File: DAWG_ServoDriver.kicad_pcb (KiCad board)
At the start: 2 copper layers, 154 parts, among them CN1 Conn_02x19_Odd_Even, CN2 Conn_02x19_Odd_Even, IC1 DRV8251ADDAR, IC2 DRV8251ADDAR, IC3 DRV8251ADDAR, IC4 DRV8251ADDAR, J1 Conn_01x05, J10 Screw_Terminal_01x02, J11 Conn_01x10, J12 Conn_01x08, J13 Conn_01x05, J14 Conn_01x06, J15 Conn_01x08, J16 Screw_Terminal_01x02, J17 Conn_01x03, J18 Conn_01x03, J19 Conn_01x03, J2 Screw_Terminal_01x02, J20 Conn_01x03, J21 Conn_01x03, J22 Conn_01x03, J23 Conn_01x03, J24 Conn_01x03, J25 Conn_01x03, J26 Conn_01x03, J27 Conn_01x03, J28 Conn_01x03, J29 Conn_01x03, J3 Conn_01x05, J30 Conn_01x03, J31 Conn_01x03, J32 Conn_01x03, J33 Conn_01x03, J34 Conn_01x03, J35 Conn_01x03, J4 Conn_01x04_Pin, J5 Screw_Terminal_01x02, J6 Conn_01x03, J7 Screw_Terminal_01x02, J8 Screw_Terminal_01x02, J9 Conn_01x05, Q1 BSS138, Q10 BSS138, Q11 BSS138, Q12 BSS138, Q13 BSS138, Q14 BSS138, Q15 BSS138, Q16 BSS138, Q17 BSS138, Q18 BSS138, Q19 BSS138, Q2 BSS138, Q20 BSS138, Q3 BSS138, Q4 BSS138, Q5 BSS138, Q6 BSS138, Q7 BSS138, Q8 BSS138, Q9 BSS138, SW1 SW_Push, U1 TPS62177DQC, U2 STM32G431C8Tx, U3 LD1117S12TR_SOT223, U4 ICM-20602, U5 ICM-20602, Y1 Crystal_GND24

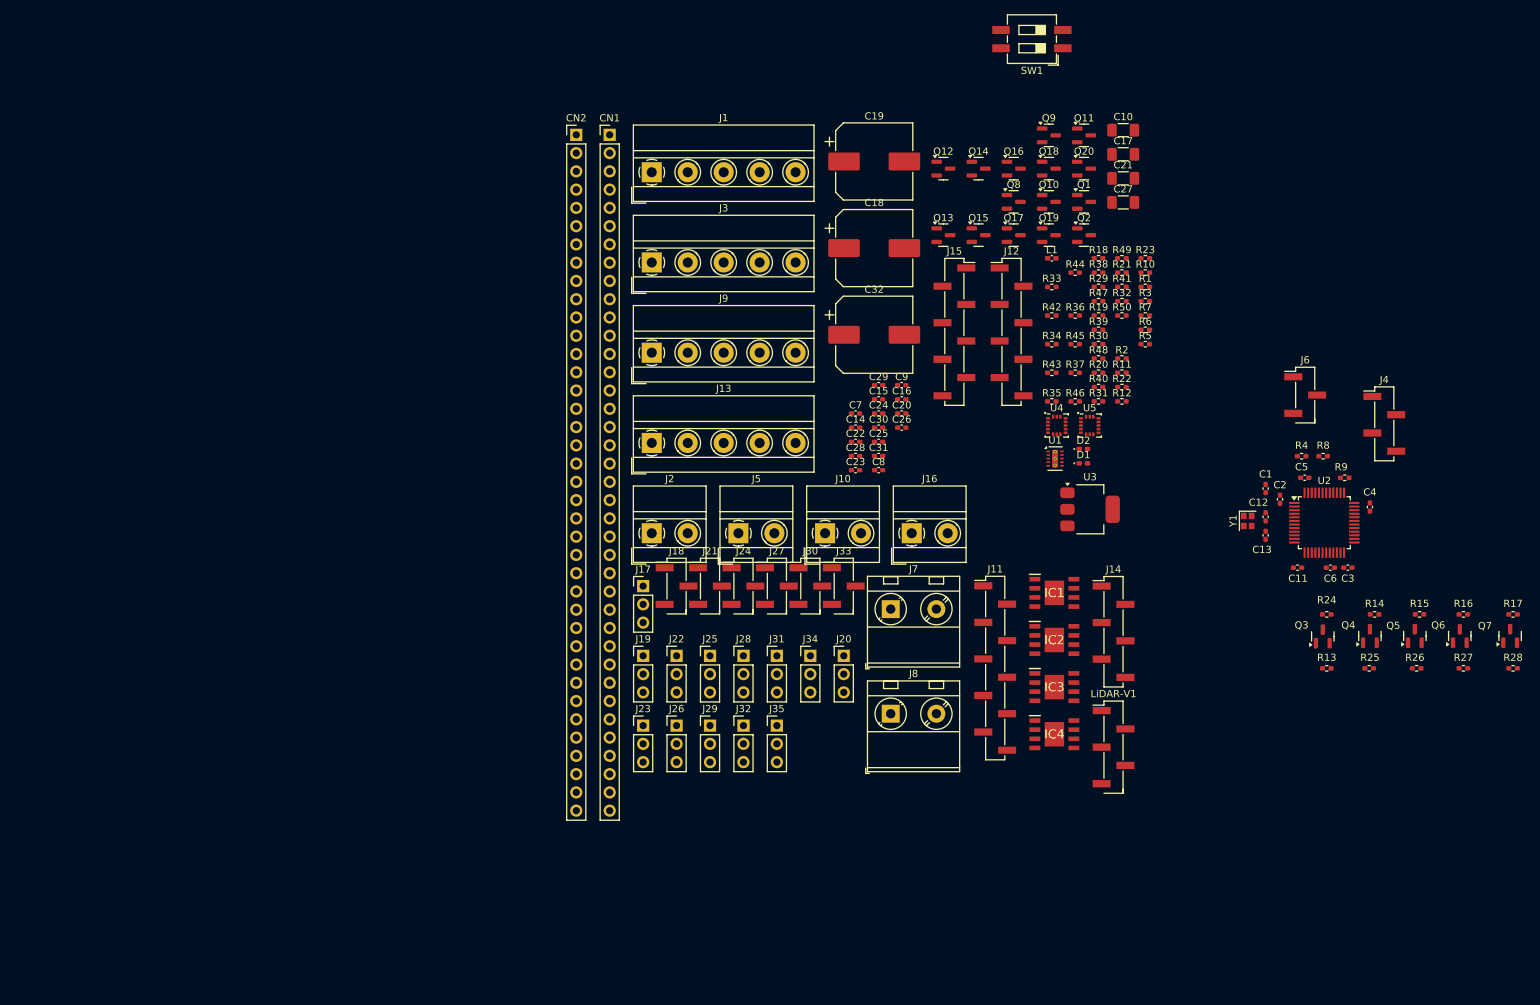
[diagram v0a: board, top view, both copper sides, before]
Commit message: Placed mos most components, routed servo.
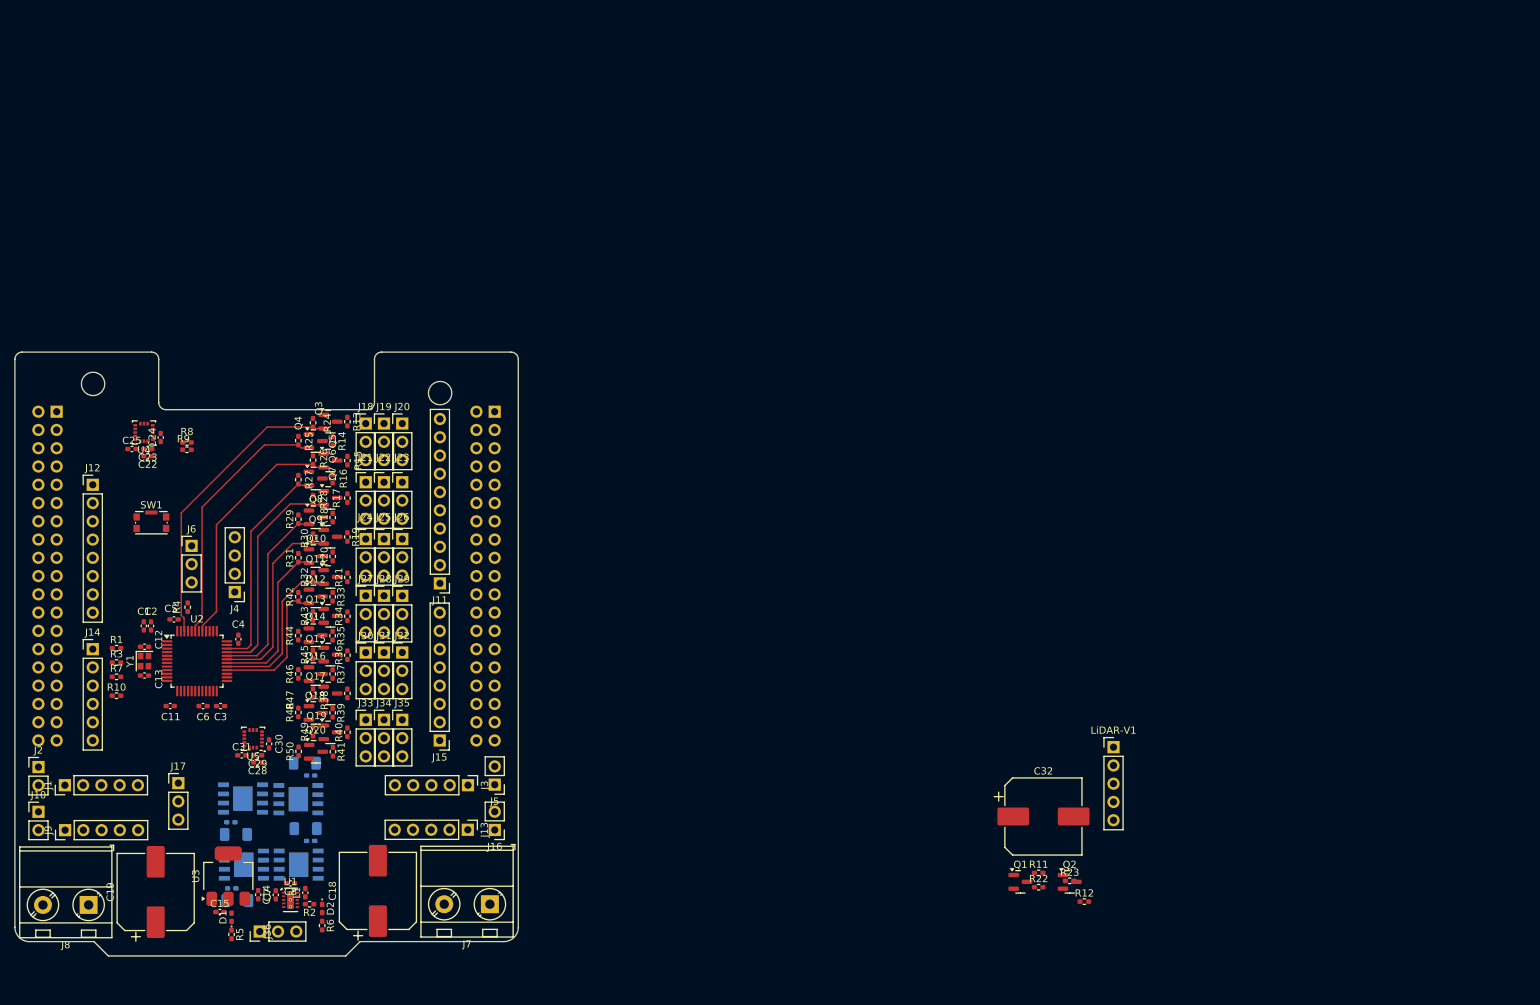
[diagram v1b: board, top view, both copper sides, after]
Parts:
- removed CN1, CN2: Conn_02x19_Odd_Even, Connector_PinHeader_2.54mm:PinHeader_1x38_P2.54mm_Vertical
- added CN10: Conn_02x19_Odd_Even, Connector_PinHeader_2.54mm:PinHeader_2x19_P2.54mm_Vertical, B.Cu at (89.8, 82.3)
- added CN7: Conn_02x19_Odd_Even, Connector_PinHeader_2.54mm:PinHeader_2x19_P2.54mm_Vertical, B.Cu at (28.9, 82.3)
- added J36: Conn_01x03, Connector_PinHeader_2.54mm:PinHeader_1x03_P2.54mm_Vertical, F.Cu at (57.1, 154.6)
- C10, C16, C17, C20, C21, C26, C27, C9, IC1, IC2, IC3, IC4: moved to B.Cu
- J1, J13, J3, J9: footprint TerminalBlock_MetzConnect:TerminalBlock_MetzConnect_Type011_RT05505HBWC_1x05_P5.00mm_Horizontal -> Connector_PinHeader_2.54mm:PinHeader_1x05_P2.54mm_Vertical
- J10, J16, J2, J5: footprint TerminalBlock_MetzConnect:TerminalBlock_MetzConnect_Type011_RT05502HBWC_1x02_P5.00mm_Horizontal -> Connector_PinHeader_2.54mm:PinHeader_1x02_P2.54mm_Vertical
- J11: footprint Connector_PinHeader_2.54mm:PinHeader_1x10_P2.54mm_Vertical_SMD_Pin1Left -> Connector_PinHeader_2.54mm:PinHeader_1x10_P2.54mm_Vertical
- J12: footprint Connector_PinHeader_2.54mm:PinHeader_1x08_P2.54mm_Vertical_SMD_Pin1Left -> Connector_PinHeader_2.54mm:PinHeader_1x08_P2.54mm_Vertical
- J14: footprint Connector_PinHeader_2.54mm:PinHeader_1x06_P2.54mm_Vertical_SMD_Pin1Left -> Connector_PinHeader_2.54mm:PinHeader_1x06_P2.54mm_Vertical
- J15: footprint Connector_PinHeader_2.54mm:PinHeader_1x08_P2.54mm_Vertical_SMD_Pin1Right -> Connector_PinHeader_2.54mm:PinHeader_1x08_P2.54mm_Vertical
- J18, J21, J24, J27, J30, J33, J6: footprint Connector_PinHeader_2.54mm:PinHeader_1x03_P2.54mm_Vertical_SMD_Pin1Left -> Connector_PinHeader_2.54mm:PinHeader_1x03_P2.54mm_Vertical
- J4: footprint Connector_PinHeader_2.54mm:PinHeader_1x04_P2.54mm_Vertical_SMD_Pin1Left -> Connector_PinHeader_2.54mm:PinHeader_1x04_P2.54mm_Vertical
- LiDAR-V1: footprint Connector_PinHeader_2.54mm:PinHeader_1x05_P2.54mm_Vertical_SMD_Pin1Left -> Connector_PinHeader_2.54mm:PinHeader_1x05_P2.54mm_Vertical
- SW1: footprint Button_Switch_SMD:SW_DIP_SPSTx02_Slide_6.7x6.64mm_W8.61mm_P2.54mm_LowProfile -> Button_Switch_SMD:SW_Push_1P1T-SH_NO_CK_KMR2xxG
- moved R28 168.5 mm to (64.5, 94.5), turned to 90 degrees
- moved Q7 165.2 mm to (67.0, 94.3), turned to 0 degrees
- moved R27 164.1 mm to (62.5, 91.8), turned to 90 degrees
- moved R17 162.9 mm to (69.3, 94.3), turned to -90 degrees
- moved J4 161.6 mm to (53.6, 107.4), turned to 180 degrees
- moved R9 161.0 mm to (47.0, 87.6)
- moved Q6 160.6 mm to (64.9, 91.6), turned to 0 degrees
- moved C21 159.0 mm to (54.0, 150.3), turned to 180 degrees
- moved C5 158.5 mm to (45.2, 111.2)
- moved C4 158.4 mm to (54.1, 114.0)
- moved R16 158.4 mm to (67.3, 91.6), turned to 90 degrees
- moved R8 158.0 mm to (47.0, 86.6)
- moved C2 158.0 mm to (42.0, 112.1)
- moved C11 157.9 mm to (44.7, 123.2)
- moved C3 157.9 mm to (51.7, 123.2)
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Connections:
- IC1 pad 1: /ADC1/14 -> /IsenseM1
- IC2 pad 1: /ADC1/15 -> /IsenseM2
- IC3 pad 1: /ADC1/9 -> /IsenseM3
- IC4 pad 1: /ADC1/7 -> /IsenseM4
- J11 pad 1: /PWM1/2_M3 -> Net-(CN10-Pin_21)
- J11 pad 3: /PWM4/1_M2 -> /Mtr1_EncoderB
- J11 pad 4: /ADC1/7 -> /PWM3/1_M1
- J11 pad 5: /PWM3/1_M1 -> /PWM2/1_M1
- J11 pad 6: /PWM2/1_M1 -> /Mtr1_EncoderA
- J11 pad 7: Net-(CN1-Pin_9) -> GND
- J14 pad 1: /PWM2/1 -> /IsenseM1
- J14 pad 2: /PWM2/2 -> /IsenseM2
- J14 pad 3: Net-(CN2-Pin_32) -> /IsenseM3
- J14 pad 4: /PWM1/2N -> /IsenseM4
- J15 pad 1: Net-(CN1-Pin_37) -> /IMU1_INT
- J15 pad 2: Net-(CN1-Pin_35) -> /IMU2_INT
- J15 pad 3: /Mtr3_EncoderA -> Net-(CN10-Pin_33)
- J15 pad 4: /Mtr3_EncoderB -> /Mtr2_EncoderB
- J15 pad 5: /PWM3/2_M4 -> /Mtr2_EncoderA
- J15 pad 6: /Mtr3_EncoderZ -> /PWM4/1_M2
- J15 pad 7: /PWM2/3_M4 -> Net-(CN10-Pin_25)
- J15 pad 8: /PWM1/1_M3 -> Net-(CN10-Pin_23)
- Q10 pad 2: /PWM2/4 -> /PWM1/1
- Q11 pad 2: /PWM3/1 -> /PWM15/2
- Q12 pad 2: /PWM3/2 -> /PWM15/1
- Q15 pad 2: /PWM4/1 -> Net-(Q15-S)
- Q16 pad 2: /PWM4/2 -> Net-(Q16-S)
- Q17 pad 2: /PWM4/4 -> Net-(Q17-S)
- Q18 pad 2: /PWM15/1 -> Net-(Q18-S)
- Q19 pad 2: /PWM15/2 -> Net-(Q19-S)
- Q20 pad 2: /PWM16/1 -> Net-(Q20-S)
- Q3 pad 2: /PWM1/1 -> /PWM4/4
- Q4 pad 2: /PWM1/2 -> /PWM4/1
- Q5 pad 2: /PWM1/3 -> /PWM16/1
- Q6 pad 2: /PWM1/4 -> /PWM4/2
- Q7 pad 2: /PWM2/1 -> /PWM1/4
- Q8 pad 2: /PWM2/2 -> /PWM1/3
- Q9 pad 2: /PWM2/3 -> /PWM1/2
- R1 pad 2: /ADC1/14 -> /IsenseM1
- R10 pad 2: /ADC1/7 -> /IsenseM4
- R24 pad 1: /PWM1/1 -> /PWM4/4
- R25 pad 1: /PWM1/2 -> /PWM4/1
- R26 pad 1: /PWM1/3 -> /PWM16/1
- R27 pad 1: /PWM1/4 -> /PWM4/2
- R28 pad 1: /PWM2/1 -> /PWM1/4
- R29 pad 1: /PWM2/2 -> /PWM1/3
- R3 pad 2: /ADC1/15 -> /IsenseM2
- R30 pad 1: /PWM2/3 -> /PWM1/2
- R31 pad 1: /PWM2/4 -> /PWM1/1
- R32 pad 1: /PWM3/1 -> /PWM15/2
- R42 pad 1: /PWM3/2 -> /PWM15/1
- R45 pad 1: /PWM4/1 -> Net-(Q15-S)
- R46 pad 1: /PWM4/2 -> Net-(Q16-S)
- R47 pad 1: /PWM4/4 -> Net-(Q17-S)
- R48 pad 1: /PWM15/1 -> Net-(Q18-S)
- R49 pad 1: /PWM15/2 -> Net-(Q19-S)
- R50 pad 1: /PWM16/1 -> Net-(Q20-S)
- R7 pad 2: /ADC1/9 -> /IsenseM3
- U2 pad 11: /PWM15/2 -> unconnected-(U2-PA3-Pad11)
- U2 pad 15: /PWM1/1 -> unconnected-(U2-PA7-Pad15)
- U2 pad 29: unconnected-(U2-PB15-Pad29) -> /PWM15/2
- U2 pad 30: /I2C3_SCL -> /PWM1/1
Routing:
- net /PWM4/4: track 0.00 -> 41.5 mm
- net /PWM4/1: track 0.00 -> 36.3 mm
- net /PWM16/1: track 0.00 -> 34.2 mm
- net /PWM1/4: track 0.00 -> 31.8 mm
- net /PWM4/2: track 0.00 -> 30.2 mm
- net /PWM1/2: track 0.00 -> 26.9 mm
- net /PWM1/3: track 0.00 -> 26.4 mm
- net /PWM1/1: track 0.00 -> 22.9 mm
- net /PWM15/2: track 0.00 -> 22.8 mm
- net /PWM15/1: track 0.00 -> 19.7 mm
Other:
- board outline added: 70 x 84 mm
- board text added: "STM32 Morpho"
- board text added: "®©®"

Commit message: Finished Routing all except IMU2_INT and GNDs
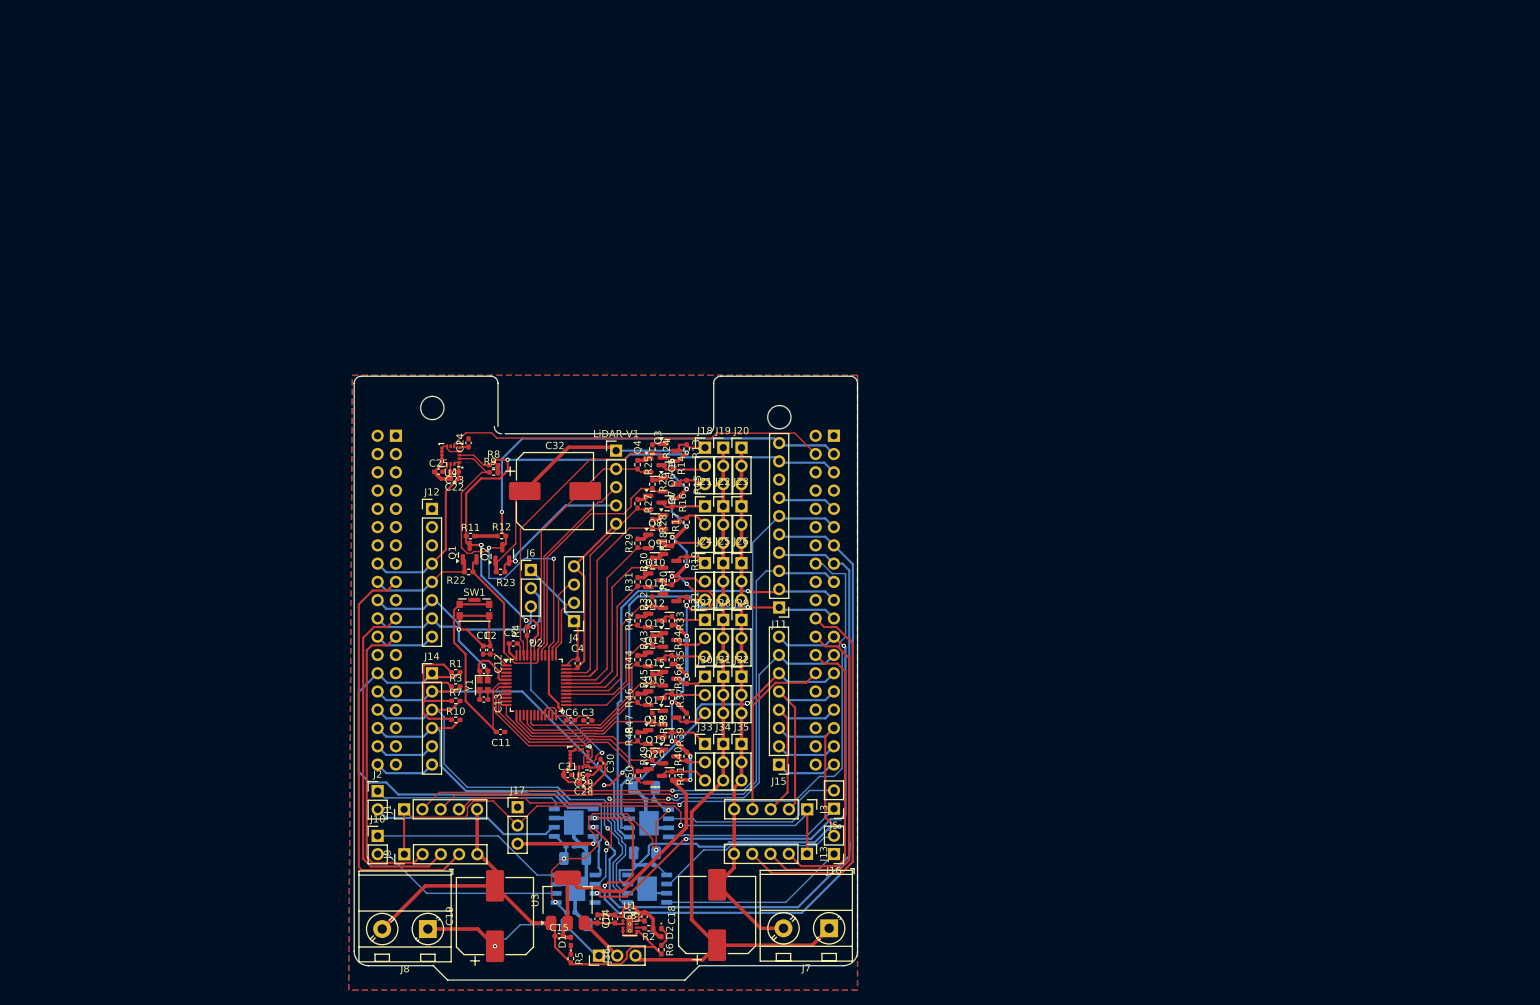
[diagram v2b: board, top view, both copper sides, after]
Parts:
- moved R12 95.7 mm to (90.8, 99.6), turned to 180 degrees
- moved R11 91.9 mm to (86.4, 99.6)
- moved Q2 91.1 mm to (90.8, 102.1), turned to 90 degrees
- moved R22 90.6 mm to (86.2, 104.6), turned to 180 degrees
- moved R23 90.1 mm to (90.6, 104.6), turned to 180 degrees
- moved Q1 89.2 mm to (86.3, 101.9), turned to 90 degrees
- moved C32 81.6 mm to (98.2, 93.3)
- moved LiDAR-V1 80.5 mm to (106.7, 87.7)
- moved C3 51.1 mm to (102.8, 125.2)
- moved C6 51.1 mm to (100.3, 125.2)
- moved IC2 48.9 mm to (111.2, 139.5)
- moved IC4 48.6 mm to (111.0, 148.6)
- moved Q3 47.3 mm to (114.1, 87.8)
- moved J4 47.3 mm to (100.8, 111.4)
- moved R13 47.3 mm to (116.5, 87.5)
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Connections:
- CN10 pad 19: /PWM3/2_M2 -> /PWM4/1_M2
- CN10 pad 2: unconnected-(CN10-Pin_2-Pad2) -> /IMU2_INT
- CN10 pad 21: Net-(CN10-Pin_21) -> /PWM1/2_M3
- CN10 pad 22: unconnected-(CN10-Pin_22-Pad22) -> /Mtr4_EncoderZ
- CN10 pad 23: Net-(CN10-Pin_23) -> /PWM1/1_M3
- CN10 pad 24: unconnected-(CN10-Pin_24-Pad24) -> /Mtr4_EncoderB
- CN10 pad 25: Net-(CN10-Pin_25) -> /PWM2/3_M4
- CN10 pad 26: unconnected-(CN10-Pin_26-Pad26) -> /Mtr4_EncoderA
- CN10 pad 27: /PWM4/1_M2 -> /PWM3/2_M2
- CN10 pad 28: unconnected-(CN10-Pin_28-Pad28) -> /Mtr2_EncoderZ
- CN10 pad 33: Net-(CN10-Pin_33) -> /PWM3/2_M4
- CN10 pad 35: /IMU2_INT -> Net-(CN10-Pin_35)
- CN10 pad 37: /IMU1_INT -> Net-(CN10-Pin_37)
- CN10 pad 4: unconnected-(CN10-Pin_4-Pad4) -> /IMU1_INT
- CN7 pad 17: /Mtr4_EncoderA -> /Mtr3_EncoderZ
- CN7 pad 21: /Mtr4_EncoderB -> /Mtr3_EncoderB
- CN7 pad 23: /Mtr4_EncoderZ -> /Mtr3_EncoderA
- CN7 pad 32: /IsenseM3 -> /IsenseM4
- CN7 pad 34: /IsenseM4 -> /IsenseM3
- J11 pad 1: Net-(CN10-Pin_21) -> /PWM1/2_M3
- J11 pad 2: /PWM3/2_M2 -> /PWM4/1_M2
- J14 pad 3: /IsenseM3 -> /IsenseM4
- J14 pad 4: /IsenseM4 -> /IsenseM3
- J15 pad 1: /IMU1_INT -> Net-(CN10-Pin_37)
- J15 pad 2: /IMU2_INT -> Net-(CN10-Pin_35)
- J15 pad 3: Net-(CN10-Pin_33) -> /PWM3/2_M4
- J15 pad 6: /PWM4/1_M2 -> /PWM3/2_M2
- J15 pad 7: Net-(CN10-Pin_25) -> /PWM2/3_M4
- J15 pad 8: Net-(CN10-Pin_23) -> /PWM1/1_M3
- Q13 pad 2: /PWM3/3 -> /PWM2/4
- Q15 pad 2: Net-(Q15-S) -> /PWM3/3
- Q16 pad 2: Net-(Q16-S) -> /PWM3/1
- Q17 pad 2: Net-(Q17-S) -> /PWM2/1
- Q18 pad 2: Net-(Q18-S) -> /PWM3/2
- Q19 pad 2: Net-(Q19-S) -> /PWM2/3
- Q20 pad 2: Net-(Q20-S) -> /PWM2/2
- R43 pad 1: /PWM3/3 -> /PWM2/4
- R45 pad 1: Net-(Q15-S) -> /PWM3/3
- R46 pad 1: Net-(Q16-S) -> /PWM3/1
- R47 pad 1: Net-(Q17-S) -> /PWM2/1
- R48 pad 1: Net-(Q18-S) -> /PWM3/2
- R49 pad 1: Net-(Q19-S) -> /PWM2/3
- R50 pad 1: Net-(Q20-S) -> /PWM2/2
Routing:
- net GND: track 0.00 -> 338.4 mm, vias 0 -> 2
- net +5V: track 0.00 -> 166.0 mm, vias 0 -> 17
- net /I2C1_SCL: track 0.00 -> 133.2 mm, vias 0 -> 5
- net +3.3V: track 0.00 -> 118.4 mm, vias 0 -> 1
- net /I2C1_SDA: track 0.00 -> 113.8 mm, vias 0 -> 7
- net /PWM2/1_M1: track 0.00 -> 110.6 mm, vias 0 -> 2
- net V_Servo: track 0.00 -> 101.5 mm
- net /PWM3/1_M1: track 0.00 -> 99.8 mm, vias 0 -> 2
- net /Mtr1_EncoderA: track 0.00 -> 94.4 mm, vias 0 -> 1
- net /Mtr1_EncoderZ: track 0.00 -> 89.1 mm, vias 0 -> 1
- net /Mtr1_EncoderB: track 0.00 -> 86.0 mm, vias 0 -> 1
- net V_DCMTR: track 0.00 -> 79.3 mm, vias 0 -> 5
- net /V_encoder: track 0.00 -> 76.8 mm, vias 0 -> 4
- net /IsenseM4: track 0.00 -> 75.8 mm
- net /PWM1/1_M3: track 0.00 -> 73.6 mm, vias 0 -> 3
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- added copper zone on B.Cu, net GND
- added copper zone on F.Cu, net GND
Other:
- outline, holes or cut-outs redrawn

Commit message: Merges pull request
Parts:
- J10, J16, J2, J5, R1, R10, R3, R7: moved to B.Cu
- moved CN7 149.0 mm to (219.3, 44.6)
- moved R5 147.0 mm to (190.4, 42.1), turned to 180 degrees
- moved D1 146.6 mm to (192.8, 42.1), turned to 0 degrees
- moved R6 144.9 mm to (201.2, 42.1), turned to 180 degrees
- moved D2 144.6 mm to (203.6, 42.1), turned to 0 degrees
- moved SW1 138.4 mm to (210.2, 46.8)
- moved J14 138.1 mm to (212.8, 77.4)
- moved J9 137.9 mm to (211.5, 112.4)
- moved J12 137.8 mm to (212.6, 54.6)
- moved J1 132.0 mm to (166.8, 40.6), turned to -90 degrees
- moved J10 122.7 mm to (191.8, 108.4)
- moved C31 117.3 mm to (180.8, 47.8), turned to 180 degrees
- moved C28 113.7 mm to (181.8, 52.7), turned to 0 degrees
- moved U5 113.1 mm to (181.3, 50.3)
- moved J36 112.6 mm to (200.0, 98.7), turned to 180 degrees
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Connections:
- CN10 pad 13: /PWM2/1_M1 -> /PWM3/1_M1
- CN10 pad 15: /PWM3/1_M1 -> /PWM2/1_M1
- CN10 pad 16: /Mtr1_EncoderZ -> /Mtr1_EncoderB
- CN10 pad 17: /Mtr1_EncoderB -> /Mtr1_EncoderZ
- CN10 pad 21: /PWM1/2_M3 -> /PWM3/2_M2
- CN10 pad 23: /PWM1/1_M3 -> /PWM1/2_M3
- CN10 pad 25: /PWM2/3_M4 -> /PWM1/1_M3
- CN10 pad 27: /PWM3/2_M2 -> /PWM2/3_M4
- CN10 pad 28: /Mtr2_EncoderZ -> /Mtr2_EncoderB
- CN10 pad 31: /Mtr2_EncoderB -> /Mtr2_EncoderZ
- CN7 pad 32: /IsenseM4 -> /IsenseM3
- CN7 pad 34: /IsenseM3 -> /IsenseM4
- J11 pad 1: /PWM1/2_M3 -> /PWM3/2_M2
- J11 pad 3: /Mtr1_EncoderB -> /Mtr1_EncoderZ
- J11 pad 4: /PWM3/1_M1 -> /PWM2/1_M1
- J11 pad 5: /PWM2/1_M1 -> /PWM3/1_M1
- J14 pad 3: /IsenseM4 -> /IsenseM3
- J14 pad 4: /IsenseM3 -> /IsenseM4
- J15 pad 4: /Mtr2_EncoderB -> /Mtr2_EncoderZ
- J15 pad 6: /PWM3/2_M2 -> /PWM2/3_M4
- J15 pad 7: /PWM2/3_M4 -> /PWM1/1_M3
- J15 pad 8: /PWM1/1_M3 -> /PWM1/2_M3
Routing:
- net GND: track 338.4 -> 9.08 mm, vias 2 -> 0
- net +5V: track 166.0 -> 4.17 mm, vias 17 -> 0
- net +3.3V: track 118.4 -> 4.17 mm, vias 1 -> 0
- net /I2C1_SCL: track 133.2 -> 36.1 mm, vias 5 -> 0
- net /I2C1_SDA: track 113.8 -> 21.6 mm, vias 7 -> 0
- net V_DCMTR: track 79.3 -> 0.00 mm, vias 5 -> 0
- net /Mtr1_EncoderA: track 94.4 -> 21.4 mm, vias 1 -> 0
- net /Mtr1_EncoderB: track 86.0 -> 26.9 mm, vias 1 -> 0
- net /PWM2/1_M1: track 110.6 -> 53.7 mm, vias 2 -> 0
- net /Mtr1_EncoderZ: track 89.1 -> 35.9 mm, vias 1 -> 0
- net /IMU1_INT: track 53.0 -> 0.00 mm
- net V_Servo: track 101.5 -> 53.7 mm
- net /PWM3/1_M1: track 99.8 -> 54.9 mm, vias 2 -> 0
- net /PWM4/4: track 42.6 -> 0.00 mm
- net /Mtr2_EncoderZ: track 25.1 -> 55.9 mm
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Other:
- board size 70 x 84 mm -> 70.2 x 84 mm
- board text added: "${REFERENCE}"
- board text removed: "®©®"
